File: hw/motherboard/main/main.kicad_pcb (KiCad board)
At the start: 4 copper layers, 100 x 100 mm, 132 parts, among them J1 SWD holes, J10 stack[0..3], J11 stack[0..3], J12 stack[0..3], J13 GPIO, J2 Conn_ARM_JTAG_SWD_10, J3 690-005-299-043, J4 STACK_GND, J5 RGB stack, J6 5V power in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

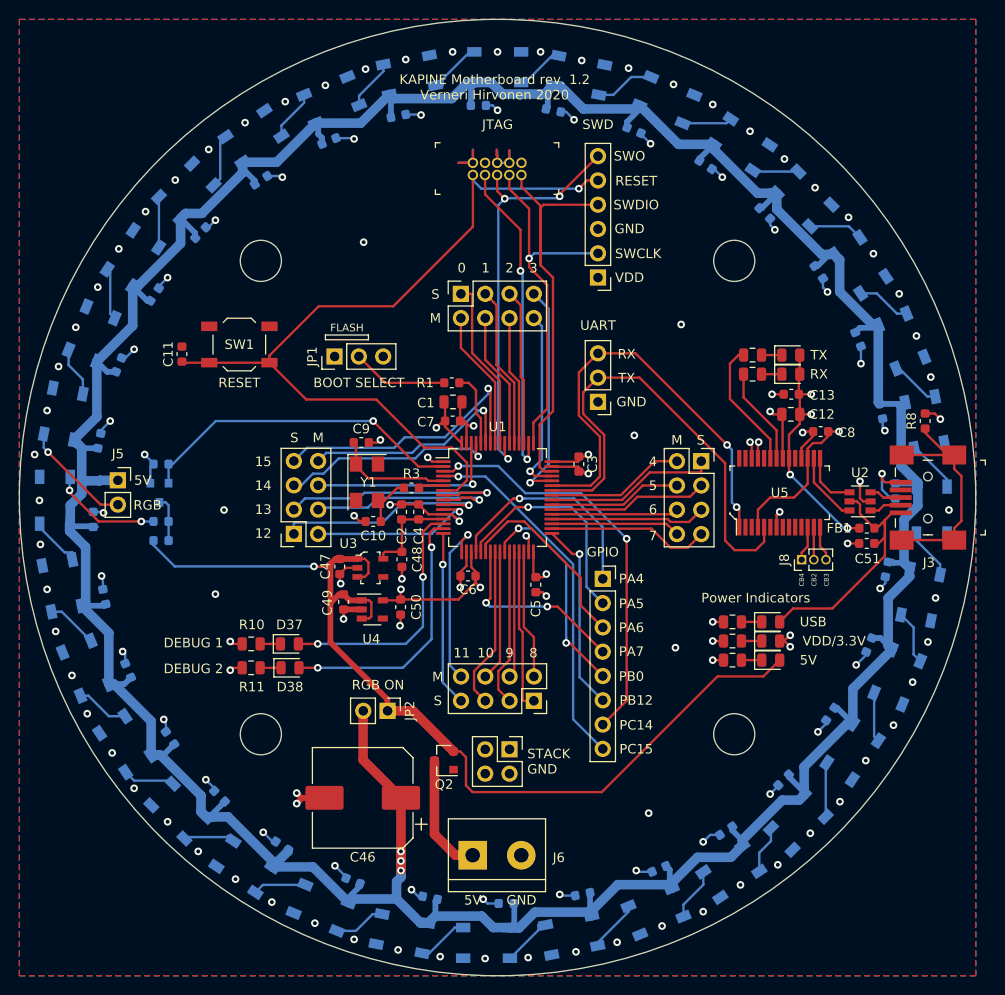
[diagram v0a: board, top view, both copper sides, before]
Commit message: Finish laying out relelauta v2.0 PCB. Minor tweaks to motherboard.
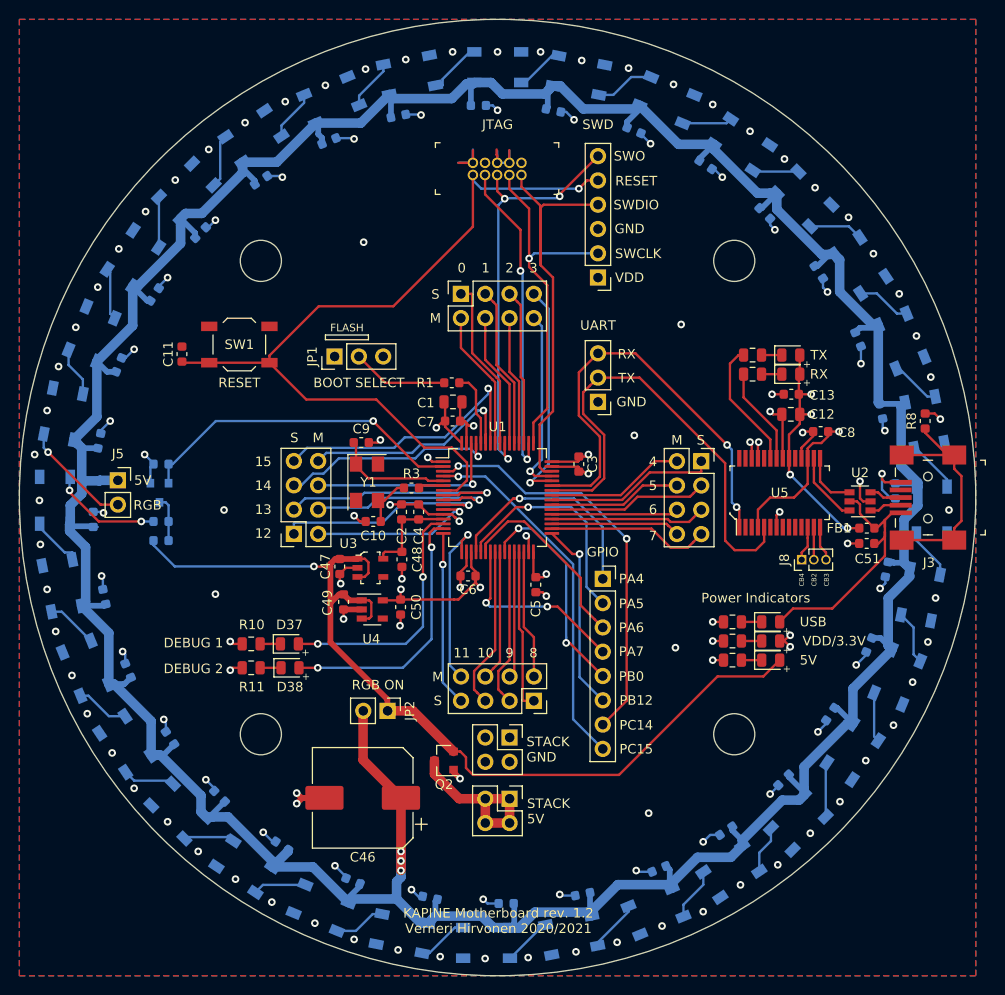
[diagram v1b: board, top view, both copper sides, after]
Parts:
- J6: value 5V power in -> STACK_5V; footprint TerminalBlock:TerminalBlock_bornier-2_P5.08mm -> Connector_PinSocket_2.54mm:PinSocket_2x02_P2.54mm_Vertical
- moved J6 7.06 mm to (151.3, 131.5)
- moved J4 1.24 mm to (151.3, 125.1)
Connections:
- J6 pad 1: Net-(J6-Pad1) -> /power/5V_in
- J6 pad 2: GND -> /power/5V_in
- Q2 pad 3: Net-(J6-Pad1) -> /power/5V_in
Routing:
- net /power/5V_in: track 0.00 -> 18.0 mm
- net Net-(J6-Pad1): track 12.6 -> 0.00 mm
- net +5V: track 104.3 -> 101.8 mm
- net GND: track 144.6 -> 145.8 mm, vias 129 -> 130
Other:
- board text added: "+"
- board text added: "KAPINE Motherboard rev. 1.2 Verneri Hirvonen 2020/2021"
- board text added: "STACK 5V"
- board text removed: "KAPINE Motherboard rev. 1.2 Verneri Hirvonen 2020"

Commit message: Board layouts before checking gerbers for alignment
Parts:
- J13: footprint Connector_PinSocket_2.54mm:PinSocket_1x08_P2.54mm_Vertical -> Connector_PinHeader_2.54mm:PinHeader_2x04_P2.54mm_Vertical
- J4, J6: footprint Connector_PinSocket_2.54mm:PinSocket_2x02_P2.54mm_Vertical -> Connector_PinSocket_2.54mm:PinSocket_1x02_P2.54mm_Vertical
- moved J6 14.9 mm to (158.9, 118.7)
- moved J4 12.0 mm to (141.1, 118.7)
- moved Q2 6.53 mm to (150.9, 126.8), turned to 0 degrees
- moved J13 3.22 mm to (164.1, 107.7)
- moved JP2 2.64 mm to (135.9, 122.9)
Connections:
- J13 pad 5: /PB0 -> /PC15
- J13 pad 6: /PB12 -> /PC14
- J13 pad 7: /PC14 -> /PB12
- J13 pad 8: /PC15 -> /PB0
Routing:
- net /PC15: track 38.0 -> 26.0 mm
- net /PC14: track 43.0 -> 35.1 mm, vias 2 -> 1
- net /power/5V_in: track 18.0 -> 12.8 mm
- net /PA7: track 19.8 -> 24.0 mm
- net /PB0: track 23.1 -> 26.3 mm, vias 2 -> 1
- net /PB12: track 20.1 -> 17.5 mm
- net GND: track 145.8 -> 144.2 mm, vias 130 -> 132
- net +5V: track 101.8 -> 103.1 mm
- net /PA5: track 23.4 -> 24.4 mm
- net /DEBUG_2: track 27.9 -> 27.3 mm
- net /rgb/5V_RGB: track 413.6 -> 414.1 mm
- net /PA4: track 23.2 -> 23.6 mm, vias 1 -> 2
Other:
- board text added: "Cockroach Catcher"
- board text added: "KAPINE Motherboard Revision 1.2 Verneri Hirvonen 2020/2021 tilaaminen vähän venähti D:"
- board text removed: "KAPINE Motherboard rev. 1.2 Verneri Hirvonen 2020/2021"
- board text removed: "STACK 5V"
- board text removed: "STACK GND"
